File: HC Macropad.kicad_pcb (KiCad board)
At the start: 2 copper layers, 173.2 x 57 mm, 65 parts, among them J1 USB_C_Receptacle_USB2.0_16P, J2 Conn_01x02_Socket, J3 Conn_01x04_Socket, J4 Conn_01x04_Socket, J5 Conn_01x04_Socket, SW1 SW_Push, U1 RP2040, U2 W25Q128JVPIQ, U3 AP2127K-3.3, U4 USBLC6-2P6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

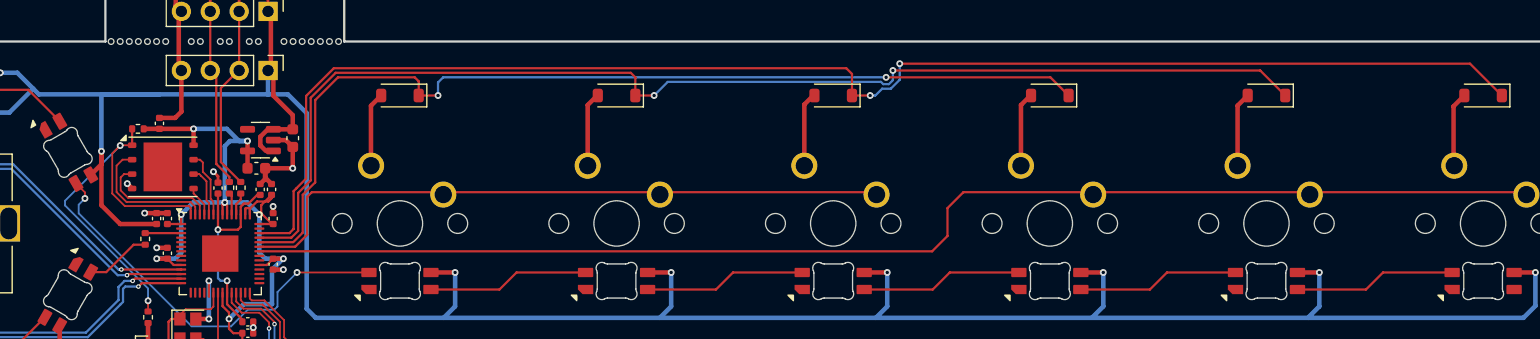
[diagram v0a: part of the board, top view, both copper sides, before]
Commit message: Pack flash a little bit more closer to the rest of the MCU components to give as much clearance to the handsolder components as possible
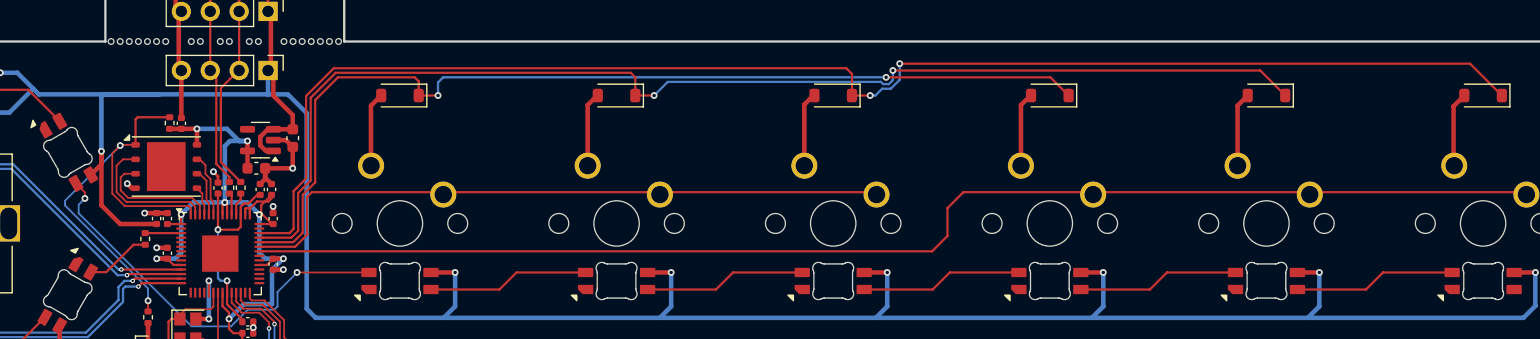
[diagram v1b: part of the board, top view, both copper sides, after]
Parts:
- moved R9 2.84 mm to (114.9, 83.9), turned to 90 degrees
- moved C10 1.93 mm to (115.9, 84.0)
- moved U2 0.30 mm to (114.6, 87.7)
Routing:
- net /MCU/QSPI_~{CS}: track 34.6 -> 38.8 mm
- net +3V3: track 101.7 -> 99.7 mm
- net GND: track 54.3 -> 53.0 mm

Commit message: Minor trace touch up
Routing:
- net GND: track 53.0 -> 53.9 mm
- net /MCU/D-: track 31.8 -> 30.9 mm
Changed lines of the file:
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@@
 	)
 	(segment
-		(start 119.15 88.6)
-		(end 119.15 89.16)
-		(width 0.25)
-		(layer "F.Cu")
-		(net 1)
-	)
-	(segment
 		(start 125.722237 87.9)
 		(end 125.722237 86.022237)
@@
 	)
 	(segment
+		(start 119.15 87.2)
+		(end 119.15 89.16)
+		(width 0.25)
+		(layer "F.Cu")
+		(net 1)
+	)
+	(segment
 		(start 116.5 105)
 		(end 116.5 104.275)
@@
 	)
 	(segment
+		(start 119.05 87.1)
+		(end 119.15 87.2)
+		(width 0.25)
+		(layer "F.Cu")
+		(net 1)
+	)
+	(segment
 		(start 118.35 98.8375)
 		(end 118.35 97.85)
@@
 		(net 1)
 	)
-	(segment
-		(start 118.75 88.2)
-		(end 119.15 88.6)
-		(width 0.25)
-		(layer "F.Cu")
-		(net 1)
-	)
 	(via
 		(at 112.7 91.84)
@@
 	)
 	(via
-		(at 118.75 88.2)
+		(at 119.05 87.1)
 		(size 0.6)
 		(drill 0.3)
@@
 	)
 	(segment
+		(start 120.1 88.615685)
+		(end 120.15 88.665685)
+		(width 0.2)
+		(layer "F.Cu")
+		(net 22)
+	)
+	(segment
 		(start 120.375 67.391116)
 		(end 120.375 68.5875)
@@
 	)
 	(segment
+		(start 118.47 79.3)
+		(end 120.1 80.93)
+		(width 0.2)
+		(layer "F.Cu")
+		(net 22)
+	)
+	(segment
+		(start 120.1 80.93)
+		(end 120.1 88.615685)
+		(width 0.2)
+		(layer "F.Cu")
+		(net 22)
+	)
+	(segment
 		(start 119 65.835)
 		(end 119 66.75)
@@
 	)
 	(segment
-		(start 120.15 88.665686)
-		(end 120.15 89.1)
-		(width 0.2)
-		(layer "F.Cu")
-		(net 22)
-	)
-	(segment
 		(start 120.2875 68.675)
 		(end 120.2875 70.375)
@@
 	)
 	(segment
-		(start 119 79.83)
-		(end 119 87.515686)
-		(width 0.2)
+		(start 120.375 68.5875)
+		(end 120.2875 68.675)
+		(width 0.25)
 		(layer "F.Cu")
 		(net 22)
 	)
 	(segment
-		(start 118.47 79.3)
-		(end 119 79.83)
+		(start 120.15 88.665685)
+		(end 120.15 89.1)
 		(width 0.2)
 		(layer "F.Cu")
@@
 	)
 	(segment
-		(start 120.375 68.5875)
-		(end 120.2875 68.675)
-		(width 0.25)
-		(layer "F.Cu")
-		(net 22)
-	)
-	(segment
 		(start 120.008884 67.025)
 		(end 120.375 67.391116)
@@
 		(net 22)
 	)
-	(segment
-		(start 119 87.515686)
-		(end 120.15 88.665686)
-		(width 0.2)
-		(layer "F.Cu")
-		(net 22)
-	)
 	(via
 		(at 120.2875 69.2)
@@
 	)
 	(segment
-		(start 119.4 87.35)
-		(end 121.15 89.1)
+		(start 121.01 79.3)
+		(end 120.95 79.3)
 		(width 0.2)
 		(layer "F.Cu")
@@
 	)
 	(segment
+		(start 120.5 88.45)
+		(end 121.15 89.1)
+		(width 0.2)
+		(layer "F.Cu")
+		(net 25)
+	)
+	(segment
+		(start 120.5 79.75)
+		(end 120.5 88.45)
+		(width 0.2)
+		(layer "F.Cu")
+		(net 25)
+	)
+	(segment
 		(start 119.5 65.835)
 		(end 119.5 67.016116)
@@
 	)
 	(segment
-		(start 119.4 80.85)
-		(end 119.4 87.35)
-		(width 0.2)
-		(layer "F.Cu")
-		(net 25)
-	)
-	(segment
 		(start 121.01 74.1)
 		(end 121.01 79.3)
@@
 	)
 	(segment
-		(start 120.95 79.3)
-		(end 119.4 80.85)
-		(width 0.2)
-		(layer "F.Cu")
-		(net 25)
-	)
-	(segment
 		(start 120.5 66.87972)
 		(end 121.2 67.57972)
@@
 	)
 	(segment
-		(start 121.01 79.3)
-		(end 120.95 79.3)
+		(start 120.95 79.3)
+		(end 120.5 79.75)
 		(width 0.2)
 		(layer "F.Cu")
@@
 	)
 	(segment
-		(start 120.35 91.9625)
-		(end 120.35 90.32)
+		(start 120.35 90.32)
+		(end 120.15 90.12)
 		(width 0.2)
 		(layer "F.Cu")
@@
 	)
 	(segment
-		(start 120.35 90.32)
-		(end 120.15 90.12)
+		(start 120.35 91.9625)
+		(end 120.35 90.32)
 		(width 0.2)
 		(layer "F.Cu")
@@
 	)
 	(segment
-		(start 118.5 88.85)
+		(start 118.5 87.35)
 		(end 118.5 90.58785)
 		(width 0.16)
@@
 	)
 	(segment
-		(start 118.5 90.58785)
-		(end 118.75 90.83785)
-		(width 0.16)
-		(layer "F.Cu")
-		(net 60)
-	)
-	(segment
 		(start 118.75 90.83785)
 		(end 118.75 91.9625)
@@
 	)
 	(segment
-		(start 118.05 87.62)
-		(end 118.05 88.4)
+		(start 118.5 90.58785)
+		(end 118.75 90.83785)
 		(width 0.16)
 		(layer "F.Cu")
@@
 	)
 	(segment
-		(start 118.05 88.4)
-		(end 118.5 88.85)
+		(start 118.29 87.14)
+		(end 118.5 87.35)
 		(width 0.16)
 		(layer "F.Cu")
@@
 	(segment
 		(start 117 87.14)
-		(end 117.57 87.14)
-		(width 0.16)
-		(layer "F.Cu")
-		(net 60)
-	)
-	(segment
-		(start 117.57 87.14)
-		(end 118.05 87.62)
+		(end 118.29 87.14)
 		(width 0.16)
 		(layer "F.Cu")
@@
 	(segment
 		(start 117.3 88.38)
-		(end 117.520884 88.38)
+		(end 117.98 88.38)
 		(width 0.16)
 		(layer "F.Cu")
@@
 	)
 	(segment
-		(start 118.14 90.736967)
-		(end 118.35 90.946967)
+		(start 118.14 88.54)
+		(end 118.14 90.736967)
 		(width 0.16)
 		(layer "F.Cu")
@@
 	)
 	(segment
-		(start 117.520884 88.38)
-		(end 118.14 88.999116)
+		(start 118.14 90.736967)
+		(end 118.35 90.946967)
 		(width 0.16)
 		(layer "F.Cu")
@@
 	)
 	(segment
-		(start 118.14 88.999116)
-		(end 118.14 90.736967)
+		(start 117.98 88.38)
+		(end 118.14 88.54)
 		(width 0.16)
 		(layer "F.Cu")
